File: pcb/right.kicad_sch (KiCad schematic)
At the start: 76 parts, among them J201 Conn_01x06_MountingPin, SW201 SW_SPDT, SW37 SW_Push, SW38 SW_Push, SW39 SW_Push, SW40 SW_Push, SW41 SW_Push, SW42 SW_Push, SW43 SW_Push, SW44 SW_Push, SW45 SW_Push, SW46 SW_Push, SW47 SW_Push, SW48 SW_Push, SW49 SW_Push, SW50 SW_Push, SW51 SW_Push, SW52 SW_Push, SW53 SW_Push, SW54 SW_Push, SW55 SW_Push, SW56 SW_Push, SW57 SW_Push, SW58 SW_Push, SW59 SW_Push, SW60 SW_Push, SW61 SW_Push, SW62 SW_Push, SW63 SW_Push, SW64 SW_Push, SW65 SW_Push, SW66 SW_Push, SW67 SW_Push, SW68 SW_Push, SW69 SW_Push, SW70 SW_Push, SW71 SW_Push, U201 BLEMicroPro

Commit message: Adapt split keyboard PCBs for AAA battery holders
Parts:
- BT201: footprint Library:battery_holder -> Library:battery_holder_AAA_1x_P55mm
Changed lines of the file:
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@@
 			)
 		)
-		(property "Footprint" "Library:battery_holder"
+		(property "Footprint" "Library:battery_holder_AAA_1x_P55mm"
 			(at 150.495 139.446 90)
 			(effects
@@
 			)
 		)
-		(property "Datasheet" "~"
+		(property "Datasheet" "https://www.monotaro.com/p/6855/7539/"
 			(at 150.495 139.446 90)
 			(effects
@@
 			)
 		)
-		(property "Description" "Single-cell battery"
+		(property "Description" "AAA single-cell holder: GB-BH-4X1-WP"
 			(at 150.495 140.97 0)
 			(effects

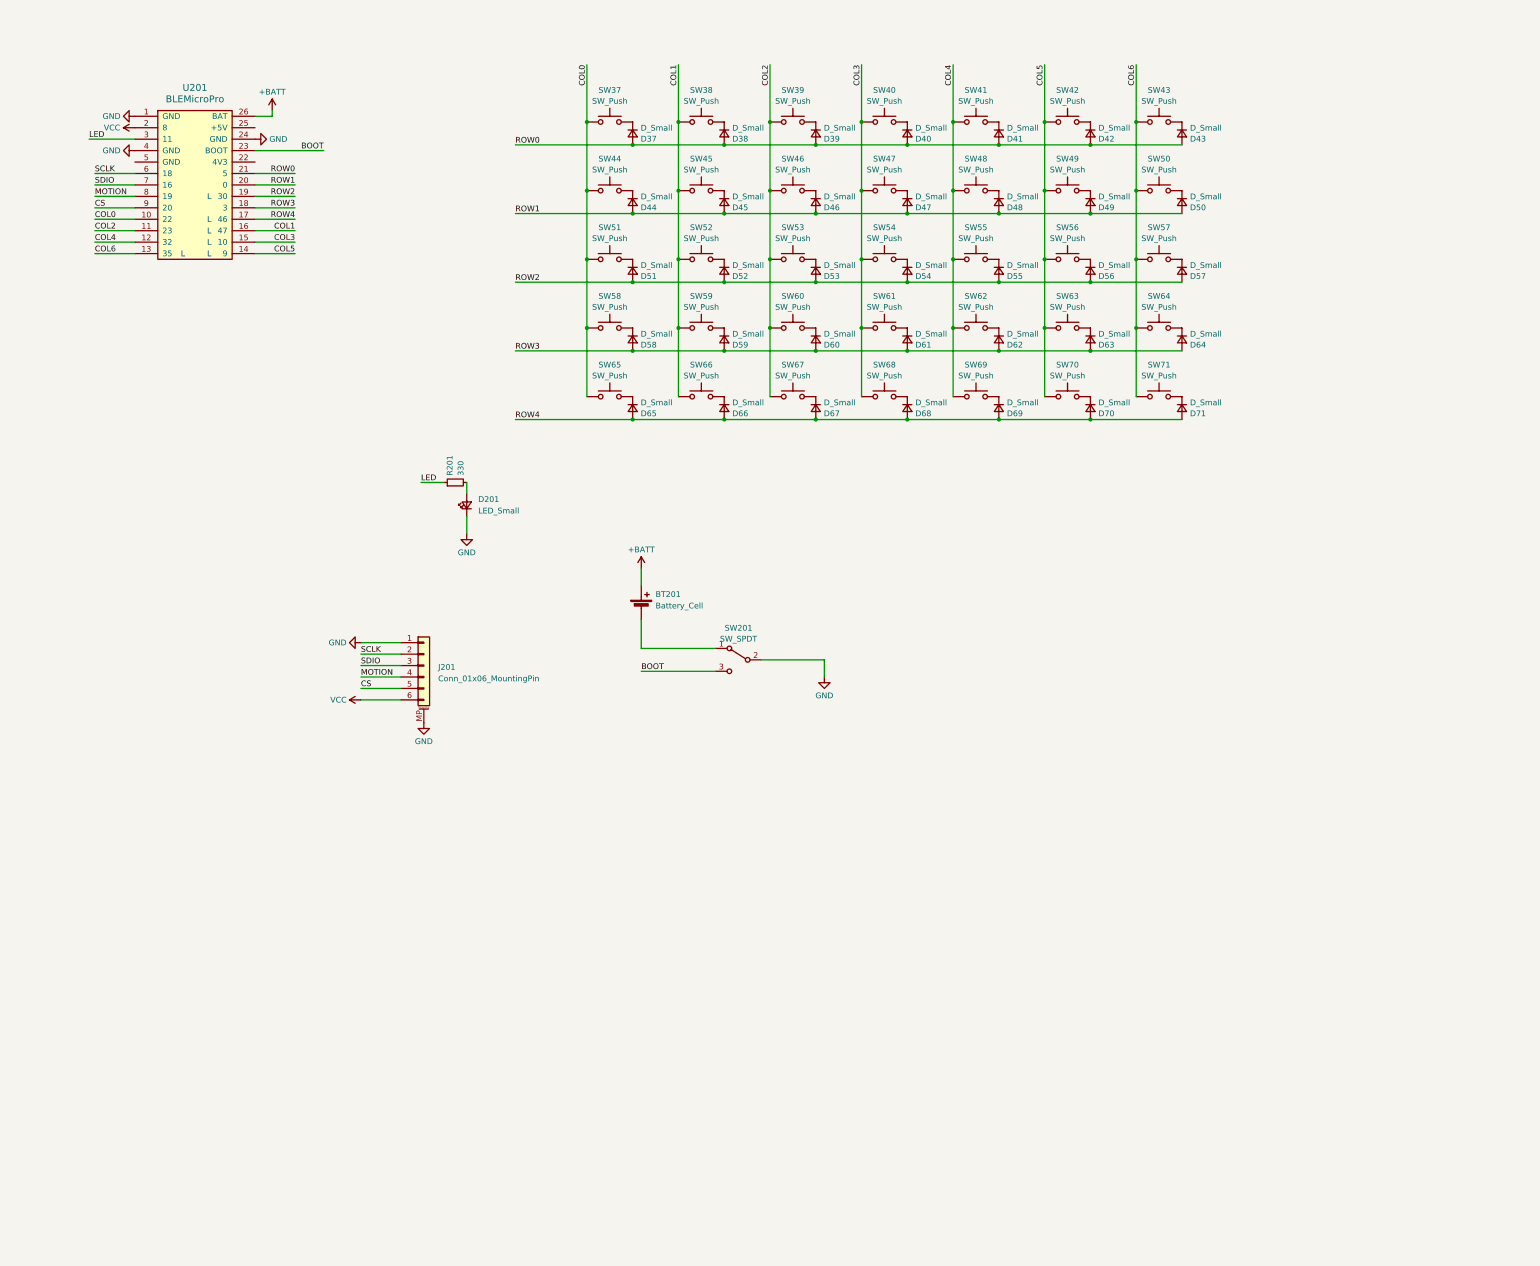
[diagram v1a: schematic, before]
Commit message: Prepare split keyboard PCBs for JLCPCB assembly
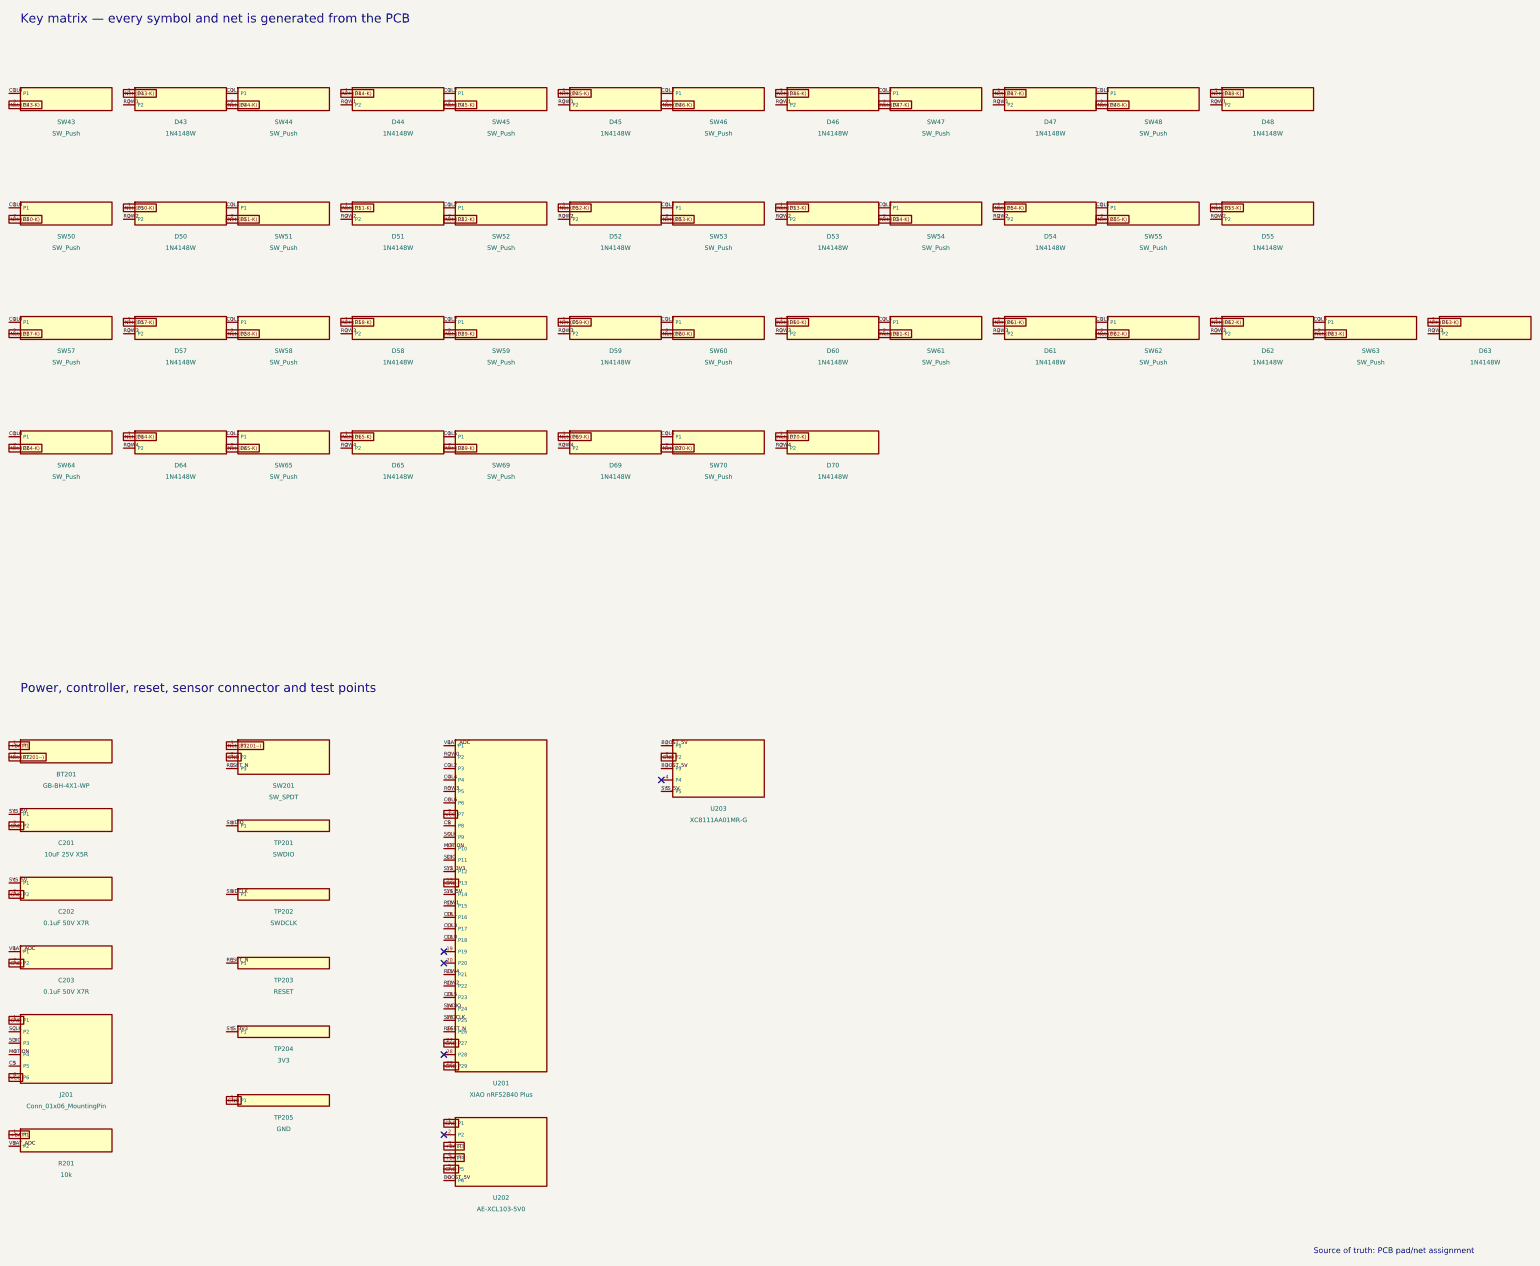
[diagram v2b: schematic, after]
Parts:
- removed BT201: Battery_Cell, Library:battery_holder_AAA_1x_P55mm, symbol Library:Battery_Cell
- removed D201: LED_Small, Library:LED_D3.0mm, symbol Library:LED_Small
- removed D37, D38, D39, D40, D41, D42, D43, D44, D45, D46, D47, D48, D49, D50, D51, D52, D53, D54, D55, D56, D57, D58, D59, D60, D61, D62, D63, D64, D65, D66, D67, D68, D69, D70, D71: D_Small, Library:D_SOD-123_HandSoldering, symbol Library:D_Small
- removed J201: Conn_01x06_MountingPin, Library:ffc-6p-adapter, symbol Library:Conn_01x06_MountingPin
- removed R201: 330, Library:R_Axial_DIN0204_L3.6mm_D1.6mm_P5.08mm_Horizontal, symbol Library:R_Small
- removed SW201: SW_SPDT, Library:ISH-1260-HA-G, symbol Library:SW_SPDT
- removed SW37, SW38, SW39, SW40, SW41, SW42, SW43, SW44, SW45, SW46, SW47, SW48, SW49, SW50, SW51, SW52, SW53, SW54, SW55, SW56, SW57, SW58, SW59, SW60, SW61, SW62, SW63, SW64, SW65, SW66, SW67, SW68, SW69, SW70, SW71: SW_Push, Library:CHOC_V2_SOCKET_HANDSOLDERING_17mm, symbol Library:SW_Push
- removed U201: BLEMicroPro, Library:BLEMicroPro, symbol Library:BLEMicroPro
- added BT201: GB-BH-4X1-WP, Library:battery_holder_AAA_1x_P55mm, symbol Torabo:Block2
- added C201: 10uF 25V X5R, Capacitor_SMD:C_0805_2012Metric, symbol Torabo:Block2
- added C202, C203: 0.1uF 50V X7R, Capacitor_SMD:C_0603_1608Metric, symbol Torabo:Block2
- added D43, D44, D45, D46, D47, D48, D50, D51, D52, D53, D54, D55, D57, D58, D59, D60, D61, D62, D63, D64, D65, D69, D70: 1N4148W, Library:D_SOD-123_HandSoldering, symbol Torabo:Block2
- added J201: Conn_01x06_MountingPin, Library:ffc-6p-adapter, symbol Torabo:Block6
- added R201: 10k, Resistor_SMD:R_0603_1608Metric, symbol Torabo:Block2
- added SW201: SW_SPDT, Library:ISH-1260-HA-G, symbol Torabo:Block3
- added SW43, SW44, SW45, SW46, SW47, SW48, SW50, SW51, SW52, SW53, SW54, SW55, SW57, SW58, SW59, SW60, SW61, SW62, SW63, SW64, SW65, SW69, SW70: SW_Push, Library:CHOC_V2_SOCKET_HANDSOLDERING_17mm, symbol Torabo:Block2
- added TP201: SWDIO, TestPoint:TestPoint_Pad_D1.5mm, symbol Torabo:Block1
- added TP202: SWDCLK, TestPoint:TestPoint_Pad_D1.5mm, symbol Torabo:Block1
- added TP203: RESET, TestPoint:TestPoint_Pad_D1.5mm, symbol Torabo:Block1
- added TP204: 3V3, TestPoint:TestPoint_Pad_D1.5mm, symbol Torabo:Block1
- added TP205: GND, TestPoint:TestPoint_Pad_D1.5mm, symbol Torabo:Block1
- added U201: XIAO nRF52840 Plus, Library:XIAO-nRF52840-Plus-SMD, symbol Torabo:Block29
- added U202: AE-XCL103-5V0, Library:AE-XCL103-5V0, symbol Torabo:Block6
- added U203: XC8111AA01MR-G, Package_TO_SOT_SMD:SOT-23-5, symbol Torabo:Block5
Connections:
- net +BATT: now also BT201.1 (P1), R201.1 (P1), U202.3 (P3), U202.4 (P4)
- net COL0: now also SW43.1 (P1), SW50.1 (P1), SW57.1 (P1), SW64.1 (P1), U201.18 (P18)
- net COL1: now also SW44.1 (P1), SW51.1 (P1), SW58.1 (P1), SW65.1 (P1), U201.16 (P16)
- net COL2: now also SW45.1 (P1), SW52.1 (P1), SW59.1 (P1), U201.3 (P3)
- net COL3: now also SW46.1 (P1), SW53.1 (P1), SW60.1 (P1), U201.17 (P17)
- net COL4: now also SW47.1 (P1), SW54.1 (P1), SW61.1 (P1), U201.4 (P4)
- net COL5: now also SW48.1 (P1), SW55.1 (P1), SW62.1 (P1), SW69.1 (P1), U201.23 (P23)
- net COL6: now also SW63.1 (P1), SW70.1 (P1), U201.6 (P6)
- net CS: now also J201.5 (P5), U201.8 (P8)
- net GND: now also C201.2 (P2), C202.2 (P2), C203.2 (P2), J201.1 (P1), SW201.2 (P2), TP205.1 (P1), U201.13 (P13), U201.27 (P27), U201.29 (P29), U202.1 (P1), U202.5 (P5), U203.2 (P2)
- net MOTION: now also J201.4 (P4), U201.10 (P10)
- net ROW0: now also U201.2 (P2)
- net ROW1: now also D43.2 (P2), D44.2 (P2), D45.2 (P2), D46.2 (P2), D47.2 (P2), D48.2 (P2), U201.15 (P15)
- net ROW2: now also D50.2 (P2), D51.2 (P2), D52.2 (P2), D53.2 (P2), D54.2 (P2), D55.2 (P2), U201.22 (P22)
- net ROW3: now also D57.2 (P2), D58.2 (P2), D59.2 (P2), D60.2 (P2), D61.2 (P2), D62.2 (P2), D63.2 (P2), U201.5 (P5)
- net ROW4: now also D64.2 (P2), D65.2 (P2), D69.2 (P2), D70.2 (P2), U201.21 (P21)
- net SCLK: now also J201.2 (P2), U201.9 (P9)
- net SDIO: now also J201.3 (P3), U201.11 (P11)
- net VCC: now also J201.6 (P6), U201.7 (P7)
- new net BOOST_5V: U202.6 (P6), U203.1 (P1), U203.3 (P3)
- new net Net-(BT201--): BT201.2 (P2), SW201.1 (P1)
- new net Net-(D43-K): D43.1 (P1), SW43.2 (P2)
- new net Net-(D44-K): D44.1 (P1), SW44.2 (P2)
- new net Net-(D45-K): D45.1 (P1), SW45.2 (P2)
- new net Net-(D46-K): D46.1 (P1), SW46.2 (P2)
- new net Net-(D47-K): D47.1 (P1), SW47.2 (P2)
- new net Net-(D48-K): D48.1 (P1), SW48.2 (P2)
- new net Net-(D50-K): D50.1 (P1), SW50.2 (P2)
- new net Net-(D51-K): D51.1 (P1), SW51.2 (P2)
- new net Net-(D52-K): D52.1 (P1), SW52.2 (P2)
- new net Net-(D53-K): D53.1 (P1), SW53.2 (P2)
- new net Net-(D54-K): D54.1 (P1), SW54.2 (P2)
- new net Net-(D55-K): D55.1 (P1), SW55.2 (P2)
- new net Net-(D57-K): D57.1 (P1), SW57.2 (P2)
- new net Net-(D58-K): D58.1 (P1), SW58.2 (P2)
- new net Net-(D59-K): D59.1 (P1), SW59.2 (P2)
- new net Net-(D60-K): D60.1 (P1), SW60.2 (P2)
- new net Net-(D61-K): D61.1 (P1), SW61.2 (P2)
- new net Net-(D62-K): D62.1 (P1), SW62.2 (P2)
- new net Net-(D63-K): D63.1 (P1), SW63.2 (P2)
- new net Net-(D64-K): D64.1 (P1), SW64.2 (P2)
- new net Net-(D65-K): D65.1 (P1), SW65.2 (P2)
- new net Net-(D69-K): D69.1 (P1), SW69.2 (P2)
- new net Net-(D70-K): D70.1 (P1), SW70.2 (P2)
- new net RESET_N: SW201.3 (P3), TP203.1 (P1), U201.26 (P26)
- new net SWDCLK: TP202.1 (P1), U201.25 (P25)
- new net SWDIO: TP201.1 (P1), U201.24 (P24)
- new net SYS_3V3: TP204.1 (P1), U201.12 (P12)
- new net SYS_5V: C201.1 (P1), C202.1 (P1), U201.14 (P14), U203.5 (P5)
- new net VBAT_ADC: C203.1 (P1), R201.2 (P2), U201.1 (P1)
- no-connect marks 0 -> 5
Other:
- note added: "Key matrix — every symbol and net is generated from the PCB"
- note added: "Power, controller, reset, sensor connector and test points"
- note added: "Source of truth: PCB pad/net assignment"
- note removed: "L"

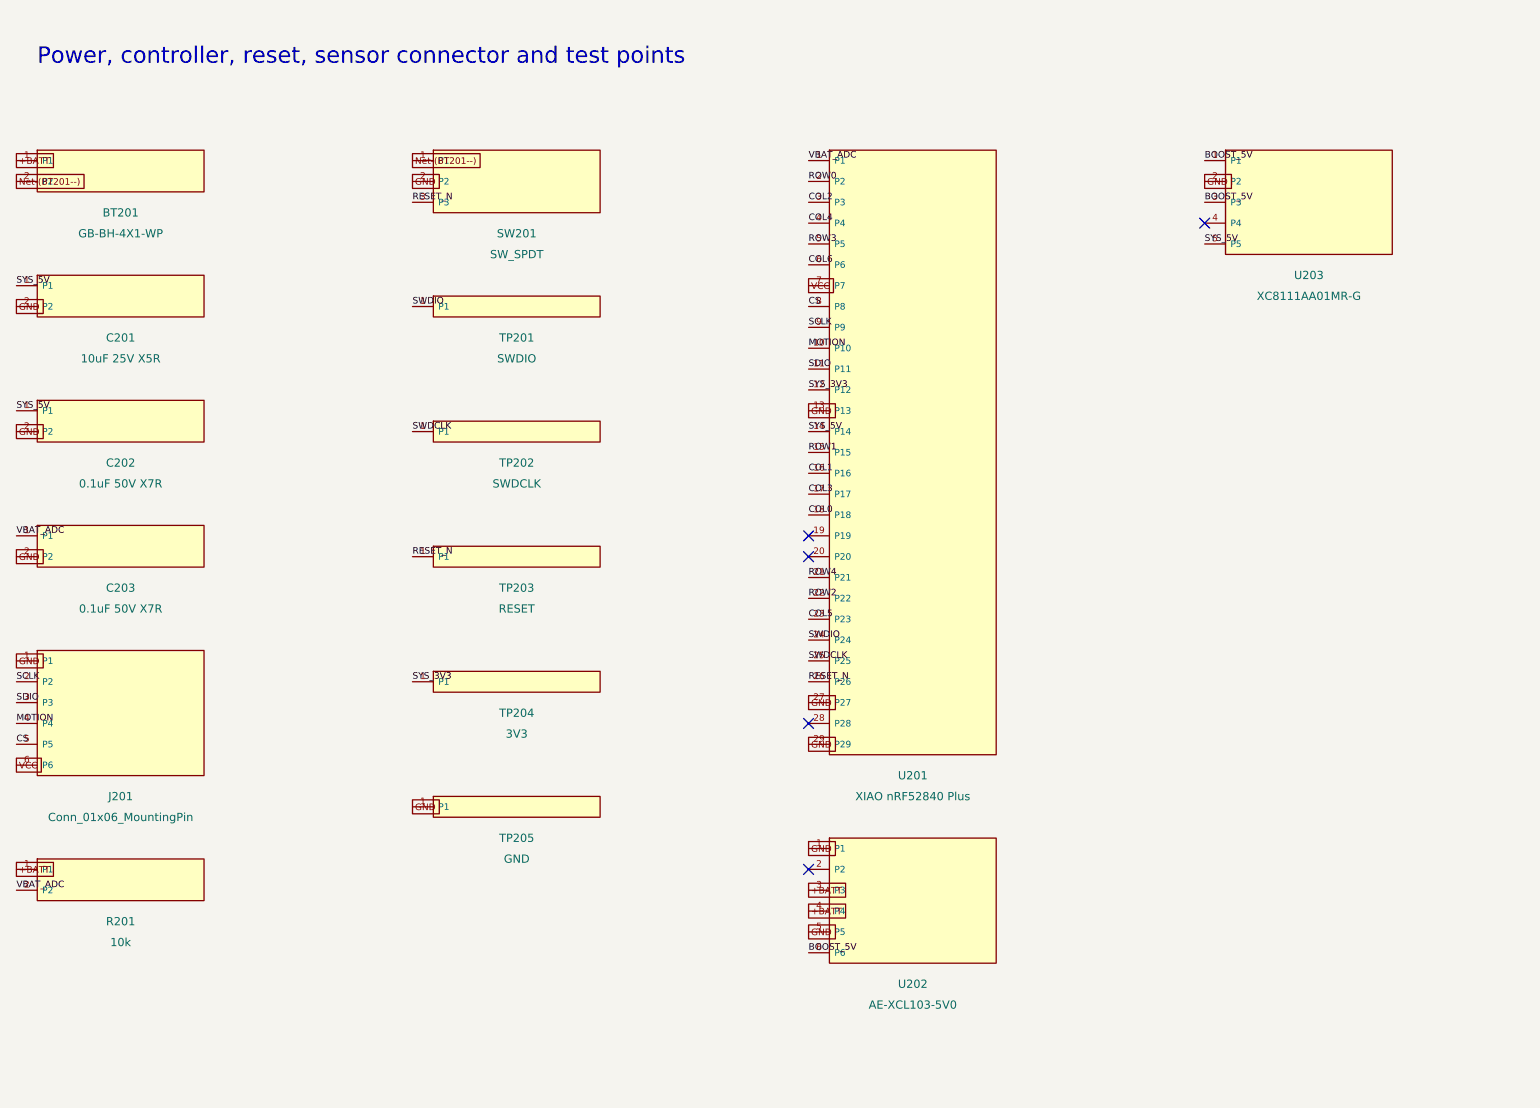
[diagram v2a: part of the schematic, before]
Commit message: Add right-side boost circuit to PCBA
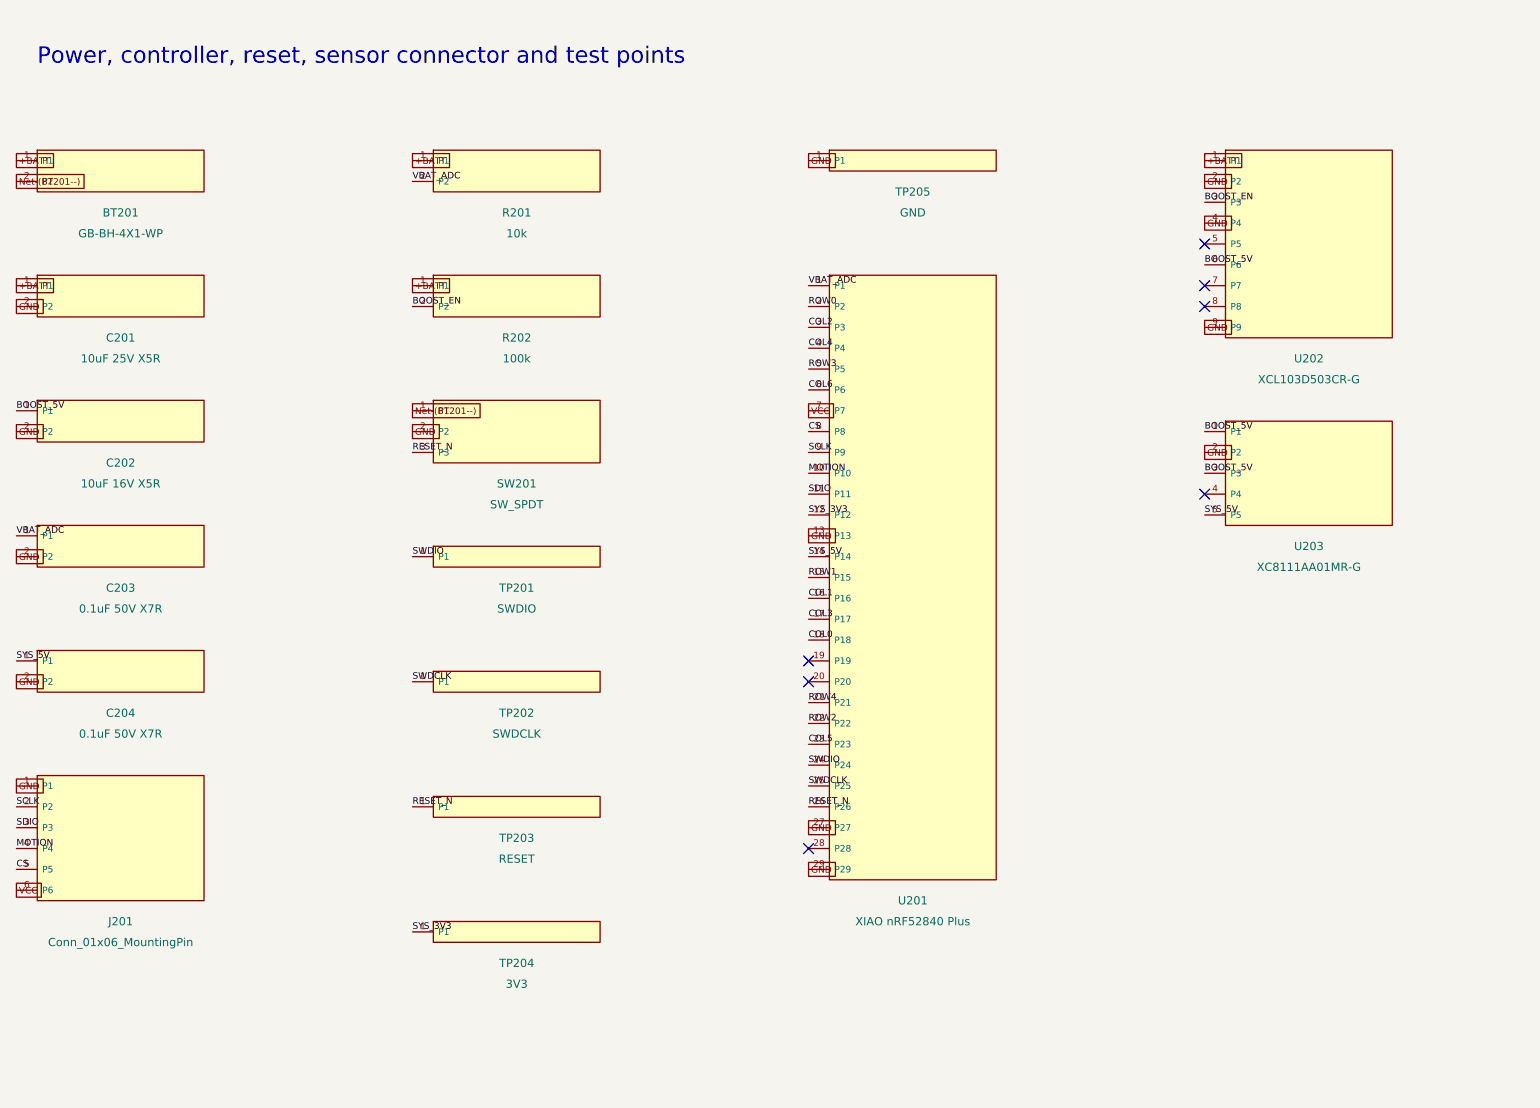
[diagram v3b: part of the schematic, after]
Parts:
- added C204: 0.1uF 50V X7R, Capacitor_SMD:C_0603_1608Metric, symbol Torabo:Block2
- added R202: 100k, Resistor_SMD:R_0603_1608Metric, symbol Torabo:Block2
- C202: value 0.1uF 50V X7R -> 10uF 16V X5R; LCSC C14663 -> C92487; MPN CC0603KRX7R9BB104 -> CL10A106MO8NQNC
- U202: value AE-XCL103-5V0 -> XCL103D503CR-G; footprint Library:AE-XCL103-5V0 -> Library:CL-2025-02; symbol Torabo:Block6 -> Torabo:Block9; LCSC (none) -> C5439677; MPN (none) -> XCL103D503CR-G
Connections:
- net +BATT: now also C201.1 (P1), U202.1 (P1), R202.1 (P1); no longer U202.3 (P3), U202.4 (P4)
- net BOOST_5V: now also C202.1 (P1)
- net GND: now also U202.2 (P2), U202.4 (P4), U202.9 (P9), C204.2 (P2); no longer U202.1 (P1), U202.5 (P5)
- net SYS_5V: now also C204.1 (P1); no longer C201.1 (P1), C202.1 (P1)
- new net BOOST_EN: R202.2 (P2), U202.3 (P3)
- no-connect marks 5 -> 7
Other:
- moved on the sheet: J201, R201, SW201, TP201, TP202, TP203, TP204, TP205, U201, U203
